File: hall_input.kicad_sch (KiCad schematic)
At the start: 10 parts, among them J2 HALL INPUT

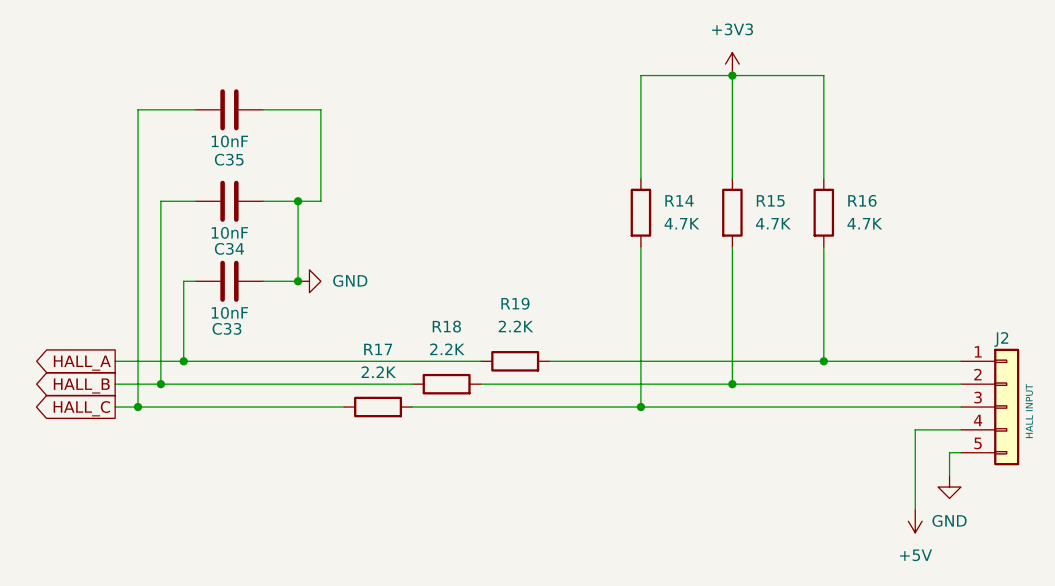
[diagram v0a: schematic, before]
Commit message: Fet Drivers  olarak IRS21867S, MOSFET olarak IAUS300N08S5N014 değiştirildi. Decoupler kısmı değiştirildi, (paraziter direnci arttırıldı.) buzzer düzeltildi ve utility kısmına alındı. CAN-BUS bitti. LDO sayısı 2x oldu
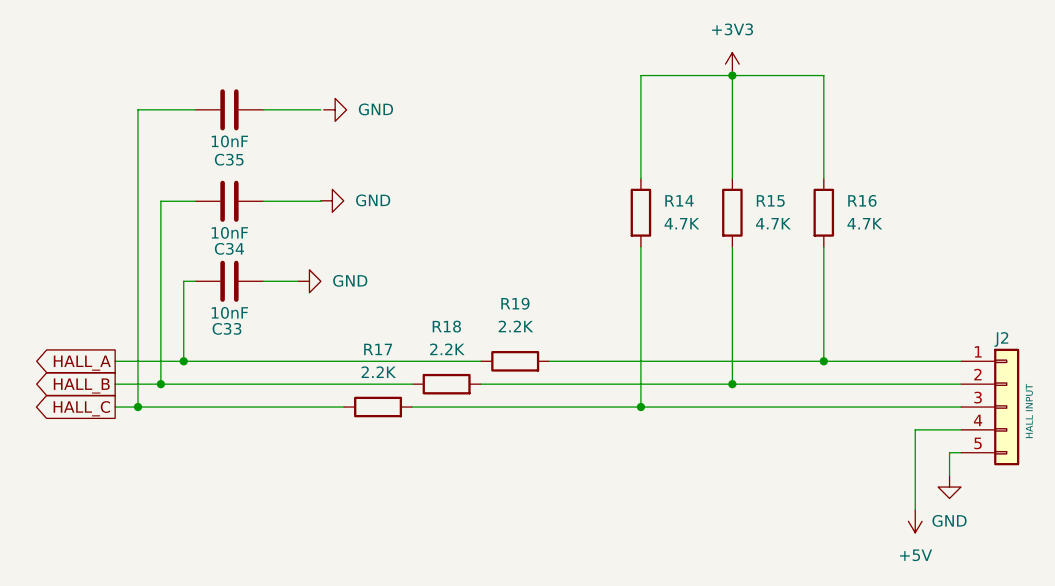
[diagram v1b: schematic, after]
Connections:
- net GND: no longer C35.2
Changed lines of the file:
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@@
 	(paper "A4")
-	(junction
-		(at 72.39 90.17)
-		(diameter 0)
-		(color 0 0 0 0)
-	)
 	(junction
 		(at 120.65 101.6)
@@
 	)
 	(junction
-		(at 72.39 81.28)
-		(diameter 0)
-		(color 0 0 0 0)
-	)
-	(junction
 		(at 54.61 104.14)
 		(diameter 0)
@@
 	(wire
 		(pts
-			(xy 74.93 81.28) (xy 72.39 81.28)
+			(xy 68.58 81.28) (xy 74.93 81.28)
 		)
 		(stroke
@@
 	(wire
 		(pts
-			(xy 68.58 81.28) (xy 72.39 81.28)
-		)
-		(stroke
-			(width 0)
-			(type default)
-		)
-	)
-	(wire
-		(pts
 			(xy 57.15 101.6) (xy 85.09 101.6)
 		)
@@
 	(wire
 		(pts
-			(xy 74.93 71.12) (xy 74.93 81.28)
-		)
-		(stroke
-			(width 0)
-			(type default)
-		)
-	)
-	(wire
-		(pts
 			(xy 130.81 78.74) (xy 130.81 67.31)
 		)
@@
 	(wire
 		(pts
-			(xy 72.39 90.17) (xy 72.39 81.28)
+			(xy 74.93 81.2296) (xy 74.93 81.28)
 		)
 		(stroke
@@
 	)
 	(symbol
+		(lib_id "power:GND")
+		(at 75.2418 71.12 90)
+		(unit 1)
+		(exclude_from_sim no)
+		(in_bom yes)
+		(on_board yes)
+		(dnp no)
+		(fields_autoplaced yes)
+		(property "Reference" "#PWR089"
+			(at 81.5918 71.12 0)
+			(effects
+				(font
+					(size 1.27 1.27)
+				)
+				(hide yes)
+			)
+		)
+		(property "Value" "GND"
+			(at 79.0518 71.1199 90)
+			(effects
+				(font
+					(size 1.27 1.27)
+				)
+				(justify right)
+			)
+		)
+		(property "Footprint" ""
+			(at 75.2418 71.12 0)
+			(effects
+				(font
+					(size 1.27 1.27)
+				)
+				(hide yes)
+			)
+		)
+		(property "Datasheet" ""
+			(at 75.2418 71.12 0)
+			(effects
+				(font
+					(size 1.27 1.27)
+				)
+				(hide yes)
+			)
+		)
+		(property "Description" "Power symbol creates a global label with name \"GND\" , ground"
+			(at 75.2418 71.12 0)
+			(effects
+				(font
+					(size 1.27 1.27)
+				)
+				(hide yes)
+			)
+		)
+		(pin "1"
+		)
+		(instances
+			(project "Motor_Driver_Shell_Eco"
+				(path "/63ef3b9c-05f1-4b00-812a-fede2372efc7/a2c879b2-b56b-45e0-81e5-a32d229bc86e"
+					(reference "#PWR089")
+					(unit 1)
+				)
+			)
+		)
+	)
+	(symbol
 		(lib_id "Connector_Generic:Conn_01x05")
 		(at 151.13 104.14 0)
@@
 					(unit 1)
 				)
+			)
+		)
+	)
+	(symbol
+		(lib_id "power:GND")
+		(at 74.93 81.2296 90)
+		(unit 1)
+		(exclude_from_sim no)
+		(in_bom yes)
+		(on_board yes)
+		(dnp no)
+		(fields_autoplaced yes)
+		(property "Reference" "#PWR085"
+			(at 81.28 81.2296 0)
+			(effects
+				(font
+					(size 1.27 1.27)
+				)
+				(hide yes)
+			)
+		)
+		(property "Value" "GND"
+			(at 78.74 81.2295 90)
+			(effects
+				(font
+					(size 1.27 1.27)
+				)
+				(justify right)
+			)
+		)
+		(property "Footprint" ""
+			(at 74.93 81.2296 0)
+			(effects
+				(font
+					(size 1.27 1.27)
+				)
+				(hide yes)
+			)
+		)
+		(property "Datasheet" ""
+			(at 74.93 81.2296 0)
+			(effects
+				(font
+					(size 1.27 1.27)
+				)
+				(hide yes)
+			)
+		)
+		(property "Description" "Power symbol creates a global label with name \"GND\" , ground"
+			(at 74.93 81.2296 0)
+			(effects
+				(font
+					(size 1.27 1.27)
+				)
+				(hide yes)
+			)
+		)
+		(pin "1"
+		)
+		(instances
+			(project "Motor_Driver_Shell_Eco"
+				(path "/63ef3b9c-05f1-4b00-812a-fede2372efc7/a2c879b2-b56b-45e0-81e5-a32d229bc86e"
+					(reference "#PWR085")
+					(unit 1)
+				)

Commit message: update Current sense
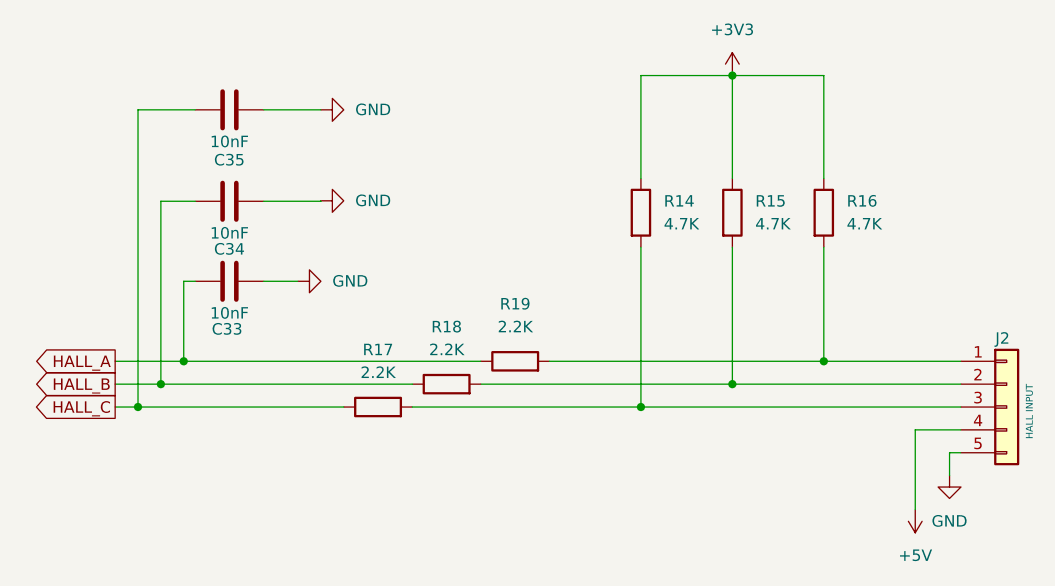
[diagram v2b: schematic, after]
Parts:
- C33, C34, C35: footprint Capacitor_THT:C_Disc_D10.5mm_W5.0mm_P5.00mm -> Capacitor_SMD:C_0603_1608Metric_Pad1.08x0.95mm_HandSolder
- R14, R15, R16, R17, R18, R19: footprint Resistor_THT:R_Axial_DIN0207_L6.3mm_D2.5mm_P7.62mm_Horizontal -> Resistor_SMD:R_0603_1608Metric_Pad0.98x0.95mm_HandSolder
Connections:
- net GND: now also C35.2
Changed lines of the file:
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@@
 			)
 		)
-		(property "Footprint" "Capacitor_THT:C_Disc_D10.5mm_W5.0mm_P5.00mm"
+		(property "Footprint" "Capacitor_SMD:C_0603_1608Metric_Pad1.08x0.95mm_HandSolder"
 			(at 68.58 80.3148 0)
 			(effects
@@
 			)
 		)
-		(property "Footprint" "Capacitor_THT:C_Disc_D10.5mm_W5.0mm_P5.00mm"
+		(property "Footprint" "Capacitor_SMD:C_0603_1608Metric_Pad1.08x0.95mm_HandSolder"
 			(at 68.58 89.2048 0)
 			(effects
@@
 		(on_board yes)
 		(dnp no)
-		(fields_autoplaced yes)
 		(property "Reference" "R16"
 			(at 133.35 81.2799 0)
@@
 			)
 		)
-		(property "Footprint" "Resistor_THT:R_Axial_DIN0207_L6.3mm_D2.5mm_P7.62mm_Horizontal"
+		(property "Footprint" "Resistor_SMD:R_0603_1608Metric_Pad0.98x0.95mm_HandSolder"
 			(at 129.032 82.55 90)
 			(effects
@@
 			)
 		)
-		(property "Footprint" "Capacitor_THT:C_Disc_D10.5mm_W5.0mm_P5.00mm"
+		(property "Footprint" "Capacitor_SMD:C_0603_1608Metric_Pad1.08x0.95mm_HandSolder"
 			(at 68.58 70.1548 0)
 			(effects
@@
 			)
 		)
-		(property "Footprint" "Resistor_THT:R_Axial_DIN0207_L6.3mm_D2.5mm_P7.62mm_Horizontal"
+		(property "Footprint" "Resistor_SMD:R_0603_1608Metric_Pad0.98x0.95mm_HandSolder"
 			(at 88.9 103.378 90)
 			(effects
@@
 			)
 		)
-		(property "Footprint" "Resistor_THT:R_Axial_DIN0207_L6.3mm_D2.5mm_P7.62mm_Horizontal"
+		(property "Footprint" "Resistor_SMD:R_0603_1608Metric_Pad0.98x0.95mm_HandSolder"
 			(at 108.712 82.55 90)
 			(effects
@@
 			)
 		)
-		(property "Footprint" "Resistor_THT:R_Axial_DIN0207_L6.3mm_D2.5mm_P7.62mm_Horizontal"
+		(property "Footprint" "Resistor_SMD:R_0603_1608Metric_Pad0.98x0.95mm_HandSolder"
 			(at 81.28 105.918 90)
 			(effects
@@
 			)
 		)
-		(property "Footprint" "Resistor_THT:R_Axial_DIN0207_L6.3mm_D2.5mm_P7.62mm_Horizontal"
+		(property "Footprint" "Resistor_SMD:R_0603_1608Metric_Pad0.98x0.95mm_HandSolder"
 			(at 96.52 100.838 90)
 			(effects
@@
 	(symbol
 		(lib_id "power:GND")
-		(at 75.2418 71.12 90)
+		(at 74.93 71.12 90)
 		(unit 1)
 		(exclude_from_sim no)
@@
 		(fields_autoplaced yes)
 		(property "Reference" "#PWR089"
-			(at 81.5918 71.12 0)
+			(at 81.28 71.12 0)
 			(effects
 				(font
@@
 		)
 		(property "Value" "GND"
-			(at 79.0518 71.1199 90)
+			(at 78.74 71.1199 90)
 			(effects
 				(font
@@
 		)
 		(property "Footprint" ""
-			(at 75.2418 71.12 0)
+			(at 74.93 71.12 0)
 			(effects
 				(font
@@
 		)
 		(property "Datasheet" ""
-			(at 75.2418 71.12 0)
+			(at 74.93 71.12 0)
 			(effects
 				(font
@@
 		)
 		(property "Description" "Power symbol creates a global label with name \"GND\" , ground"
-			(at 75.2418 71.12 0)
+			(at 74.93 71.12 0)
 			(effects
 				(font
@@
 			)
 		)
-		(property "Footprint" "Resistor_THT:R_Axial_DIN0207_L6.3mm_D2.5mm_P7.62mm_Horizontal"
+		(property "Footprint" "Resistor_SMD:R_0603_1608Metric_Pad0.98x0.95mm_HandSolder"
 			(at 118.872 82.55 90)
 			(effects
